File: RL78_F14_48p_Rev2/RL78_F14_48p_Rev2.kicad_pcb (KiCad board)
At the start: 2 copper layers, 100 x 100 mm, 52 parts, among them P1 POWER_JACKPTH, P2 E2 Lite, P3 PWR, P4 ADC, P5 F09HP, P6 USB_B, P7 Keypad, P8 RPI LCD, P9 SPI_to_eth, U1 R5F10PGJKNA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

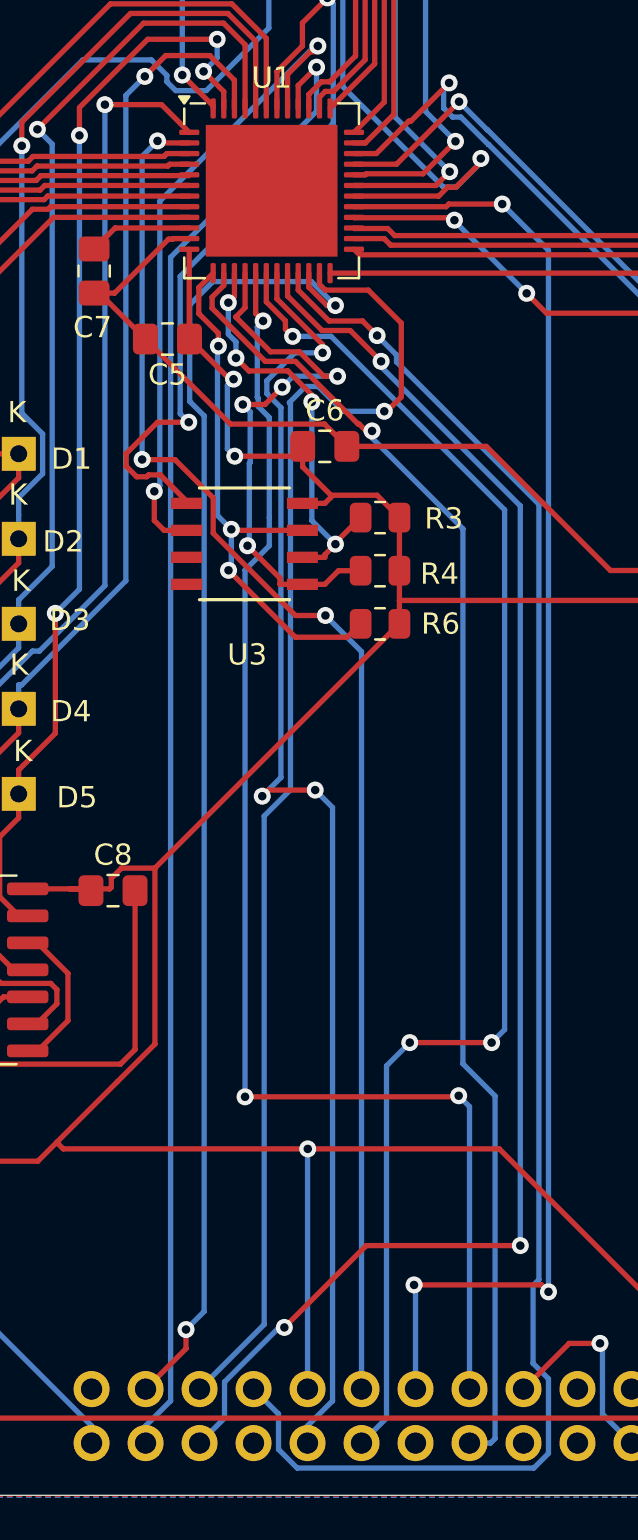
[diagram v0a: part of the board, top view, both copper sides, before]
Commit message: OOPS! P130 is write only and I had it set as input for the LCD board
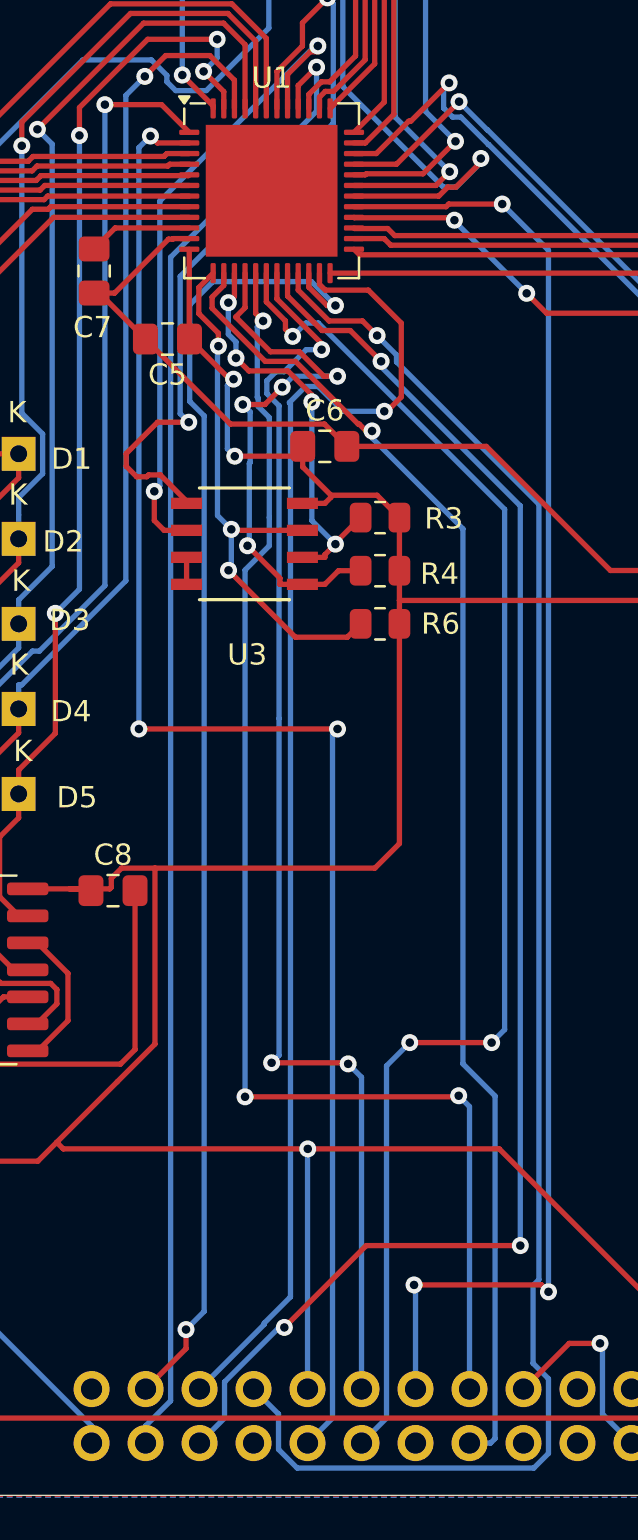
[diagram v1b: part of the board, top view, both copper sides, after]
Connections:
- U1 pad 19: /KEY3 -> /LCD_RS
- U1 pad 2: /LCD_RS -> /KEY3
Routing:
- net /KEY3: track 62.1 -> 73.8 mm
- net /LCD_RS: track 66.6 -> 59.3 mm
- net +3.3V: track 335.2 -> 341.3 mm
- net GND: track 191.4 -> 192.6 mm
- net /KEY2: track 65.8 -> 66.3 mm

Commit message: Added a few projects
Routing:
- net +3.3V: track 341.3 -> 339.1 mm
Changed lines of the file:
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@@
 		(start 89.605 158.888)
 		(end 88.15 157.432)
-		(width 0.25)
+		(width 0.5)
 		(layer "F.Cu")
 		(net 1)
@@
 		(start 90.85 146.978)
 		(end 96.405 146.978)
-		(width 0.25)
+		(width 0.5)
 		(layer "F.Cu")
 		(net 1)
@@
 		(start 95.8025 158.888)
 		(end 89.605 158.888)
-		(width 0.25)
+		(width 0.5)
 		(layer "F.Cu")
 		(net 1)
@@
 		(start 96.465 159.55)
 		(end 95.8025 158.888)
-		(width 0.25)
+		(width 0.5)
 		(layer "F.Cu")
 		(net 1)
@@
 		(start 88.15 149.575)
 		(end 90.7475 146.978)
-		(width 0.25)
+		(width 0.5)
 		(layer "F.Cu")
 		(net 1)
@@
 		(start 88.15 157.432)
 		(end 88.15 149.575)
-		(width 0.25)
+		(width 0.5)
 		(layer "F.Cu")
 		(net 1)
@@
 		(start 90.65 149.575)
 		(end 92.675 151.6)
-		(width 0.25)
+		(width 0.5)
 		(layer "F.Cu")
 		(net 2)
@@
 		(start 92.675 151.6)
 		(end 93.2 151.6)
-		(width 0.25)
+		(width 0.5)
 		(layer "F.Cu")
 		(net 2)
@@
 		(start 93.2225 151.578)
 		(end 96.4045 151.578)
-		(width 0.25)
+		(width 0.5)
 		(layer "F.Cu")
 		(net 2)
@@
 	)
 	(segment
+		(start 86.2 144)
+		(end 90.65 148.45)
+		(width 0.5)
+		(layer "B.Cu")
+		(net 2)
+	)
+	(segment
 		(start 145.1 124.875)
 		(end 143.1579 126.8171)
@@
 	)
 	(segment
+		(start 90.65 148.45)
+		(end 90.65 149.575)
+		(width 0.5)
+		(layer "B.Cu")
+		(net 2)
+	)
+	(segment
 		(start 145.1 124.03)
 		(end 145.1 124.875)
@@
 	)
 	(segment
-		(start 89.5233 149.2933)
-		(end 89.5233 149.575)
-		(width 0.25)
-		(layer "B.Cu")
-		(net 2)
-	)
-	(segment
-		(start 84.23 144)
-		(end 89.5233 149.2933)
-		(width 0.25)
-		(layer "B.Cu")
-		(net 2)
-	)
-	(segment
 		(start 144.37 161.731)
 		(end 144.37 162.54)
@@
 	(segment
 		(start 83.85 144)
-		(end 84.23 144)
-		(width 0.25)
-		(layer "B.Cu")
-		(net 2)
-	)
-	(segment
-		(start 90.65 149.575)
-		(end 89.5233 149.575)
-		(width 0.25)
+		(end 86.2 144)
+		(width 0.5)
 		(layer "B.Cu")
 		(net 2)
@@
 	)
 	(segment
-		(start 99.1 147.55)
-		(end 99.1 147.65)
-		(width 0.25)
-		(layer "F.Cu")
-		(net 4)
-	)
-	(segment
 		(start 116.318 136.468)
 		(end 116.4 136.55)
@@
 	)
 	(segment
-		(start 89.6055 156.812)
-		(end 96.2275 156.812)
-		(width 0.25)
-		(layer "F.Cu")
-		(net 4)
-	)
-	(segment
 		(start 152.72 126.57)
 		(end 151.5933 126.57)
@@
 	)
 	(segment
+		(start 89.8935 157.1)
+		(end 95.9395 157.1)
+		(width 0.5)
+		(layer "F.Cu")
+		(net 4)
+	)
+	(segment
 		(start 117.6365 145.5448)
 		(end 114.79065 148.39065)
@@
 	)
 	(segment
+		(start 95.9395 157.1)
+		(end 96.2275 156.812)
+		(width 0.5)
+		(layer "F.Cu")
+		(net 4)
+	)
+	(segment
 		(start 96.2275 156.812)
 		(end 96.465 157.05)
@@
 		(start 96.405 149.2775)
 		(end 97.472 149.2775)
-		(width 0.25)
+		(width 0.5)
 		(layer "F.Cu")
 		(net 4)
@@
 	)
 	(segment
-		(start 99.1 147.65)
-		(end 97.4725 149.278)
-		(width 0.25)
-		(layer "F.Cu")
-		(net 4)
-	)
-	(segment
 		(start 151.5933 126.57)
 		(end 147.922 122.8987)
@@
 	)
 	(segment
+		(start 89.6055 156.812)
+		(end 89.8935 157.1)
+		(width 0.5)
+		(layer "F.Cu")
+		(net 4)
+	)
+	(segment
 		(start 91.75 134.1811)
 		(end 91.75 134.99)
@@
 		(start 97.4725 149.278)
 		(end 102.7045 149.278)
-		(width 0.25)
+		(width 0.5)
 		(layer "F.Cu")
 		(net 4)
@@
 	)
 	(via
-		(at 99.1 147.55)
+		(at 99.1 149.275)
 		(size 0.8)
 		(drill 0.4)
@@
 	)
 	(segment
+		(start 99.075 149.25)
+		(end 99.075 147.525)
+		(width 0.25)
+		(layer "B.Cu")
+		(net 4)
+	)
+	(segment
 		(start 122.8181 112.7794)
 		(end 122.8181 115.7624)
@@
 	)
 	(segment
-		(start 99.1 153.2883)
-		(end 99.1 147.55)
+		(start 99.075 147.525)
+		(end 91.75 140.2)
 		(width 0.25)
 		(layer "B.Cu")
@@
 	)
 	(segment
-		(start 99.1 147.55)
-		(end 91.75 140.2)
-		(width 0.25)
-		(layer "B.Cu")
-		(net 4)
-	)
-	(segment
 		(start 147.47 96.06)
 		(end 148.9967 97.5867)
@@
 	)
 	(segment
+		(start 99.1 153.2883)
+		(end 99.1 149.275)
+		(width 0.5)
+		(layer "B.Cu")
+		(net 4)
+	)
+	(segment
 		(start 148.9967 97.5867)
 		(end 148.9967 119.4145)
@@
 		(start 96.465 157.05)
 		(end 96.465 155.9233)
+		(width 0.5)
+		(layer "B.Cu")
+		(net 4)
+	)
+	(segment
+		(start 96.465 155.9233)
+		(end 99.1 153.2883)
+		(width 0.5)
+		(layer "B.Cu")
+		(net 4)
+	)
+	(segment
+		(start 153.8865 123.537)
+		(end 153.8865 125.4035)
 		(width 0.25)
 		(layer "B.Cu")
@@
 	)
 	(segment
-		(start 96.465 155.9233)
-		(end 99.1 153.2883)
-		(width 0.25)
-		(layer "B.Cu")
-		(net 4)
-	)
-	(segment
-		(start 153.8865 123.537)
-		(end 153.8865 125.4035)
-		(width 0.25)
-		(layer "B.Cu")
+		(start 99.1 149.275)
+		(end 99.075 149.25)
+		(width 0.25)
+		(layer "B.Cu")
